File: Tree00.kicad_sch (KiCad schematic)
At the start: 4 parts, among them U21 74LS283, U3 74LS283

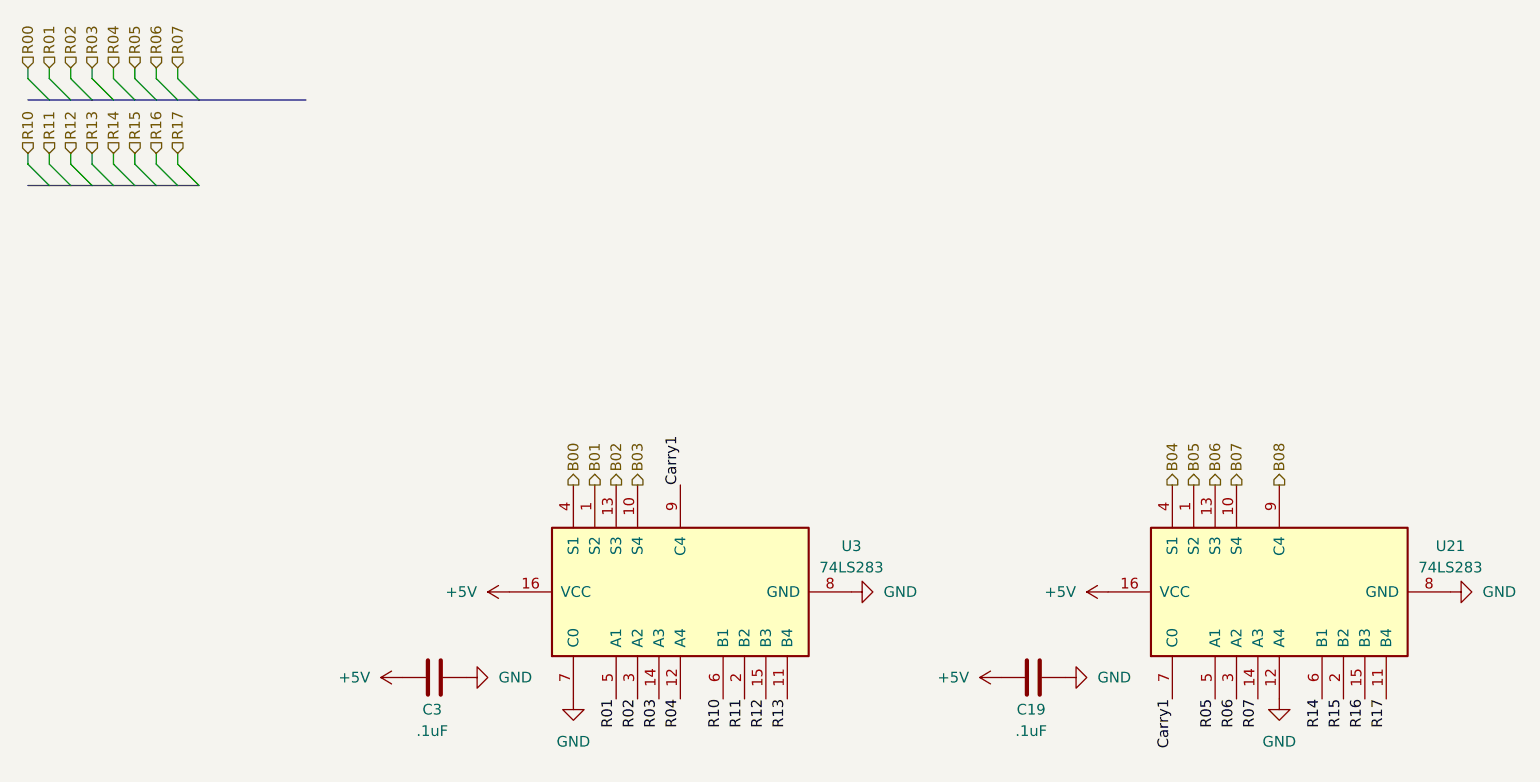
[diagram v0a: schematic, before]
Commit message: Finished schematic, need to look at power output of the mux potentially to drive LED pins, otherwise logic SHOULD be done
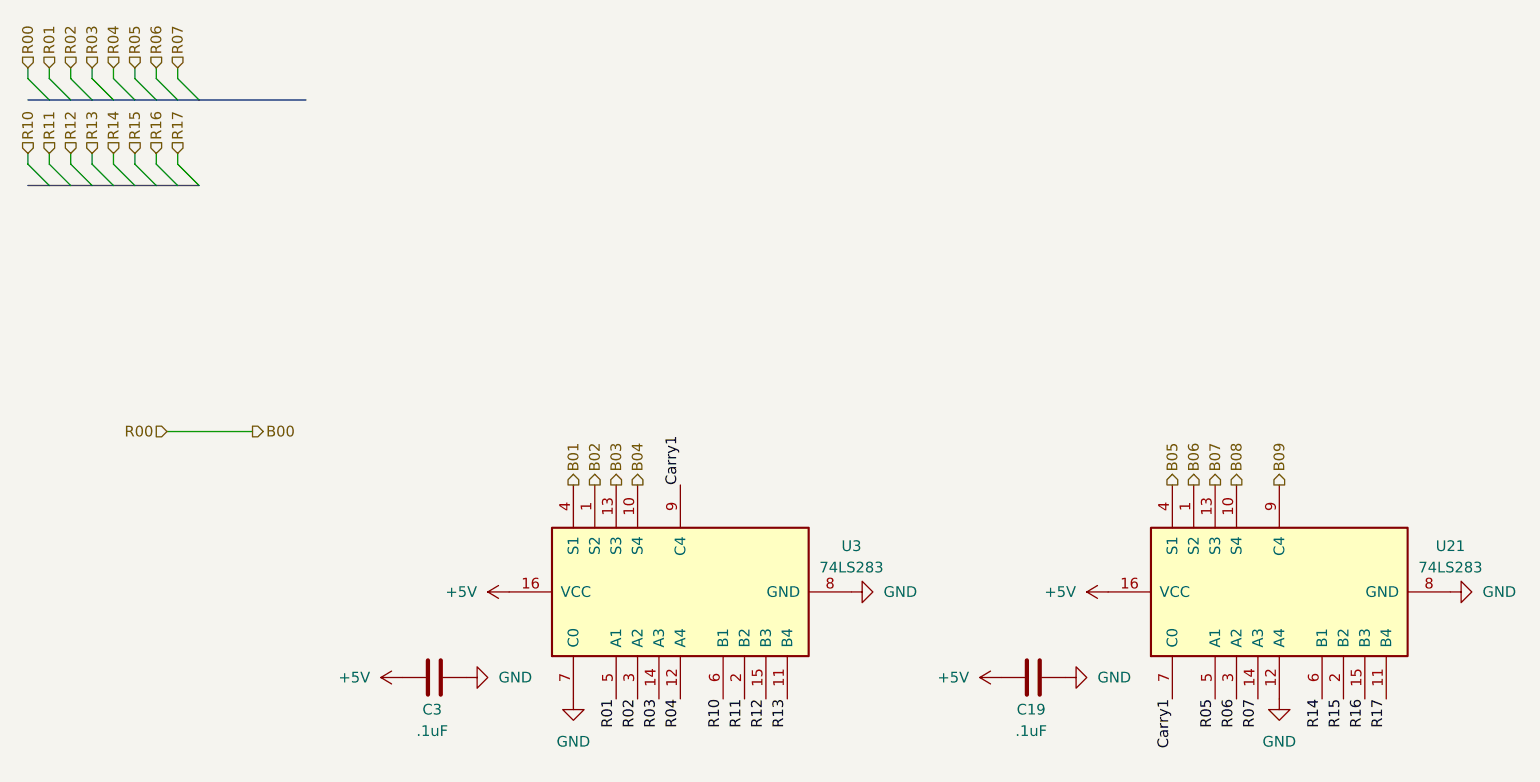
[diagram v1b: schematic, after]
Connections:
- net B00: no longer U3.4 (S1)
- net B01: now also U3.4 (S1); no longer U3.1 (S2)
- net B02: now also U3.1 (S2); no longer U3.13 (S3)
- net B03: now also U3.13 (S3); no longer U3.10 (S4)
- net B04: now also U3.10 (S4); no longer U21.4 (S1)
- net B05: now also U21.4 (S1); no longer U21.1 (S2)
- net B06: now also U21.1 (S2); no longer U21.13 (S3)
- net B07: now also U21.13 (S3); no longer U21.10 (S4)
- net B08: now also U21.10 (S4); no longer U21.9 (C4)
- new net B09: U21.9 (C4)

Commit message: Fixed ERC issues and applied Footprints
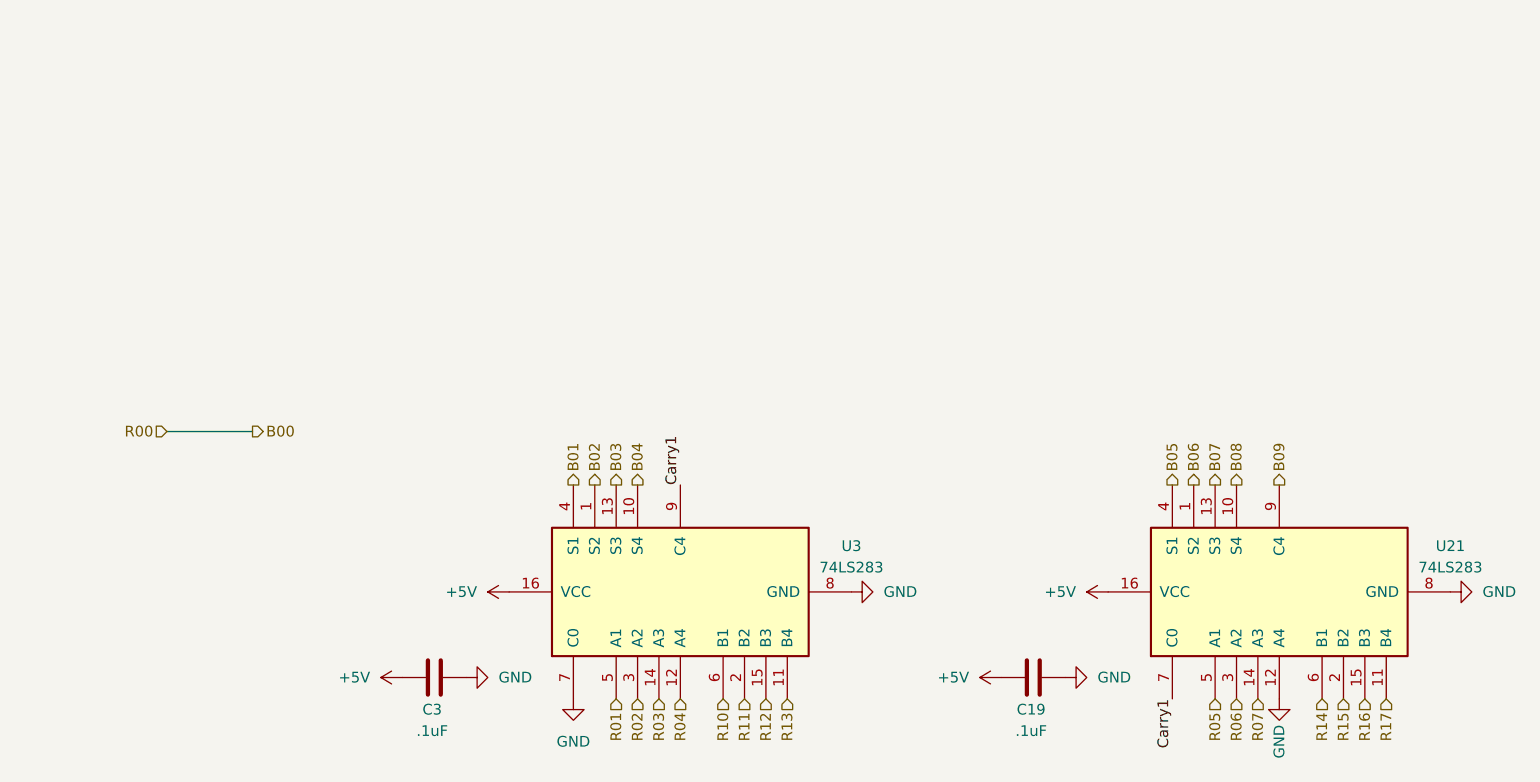
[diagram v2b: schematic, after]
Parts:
- C19, C3: footprint (none) -> Capacitor_SMD:C_0402_1005Metric
- U21, U3: footprint (none) -> Package_SO:SOIC-16_3.9x9.9mm_P1.27mm
